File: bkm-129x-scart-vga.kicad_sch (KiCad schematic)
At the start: 58 parts, among them J1 DB15_Female_HighDensity_Mount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, J2 SCART-F, J3 SJ1-353XNG, J5 Conn_02x32_Row_Letter_Last, Q1 DTC144EKA, Q2 MMBT3904, SW1 PBH4UEENAGX, SW2 PBH4UEENAGX, U1 ADG1611, U2 THS7374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

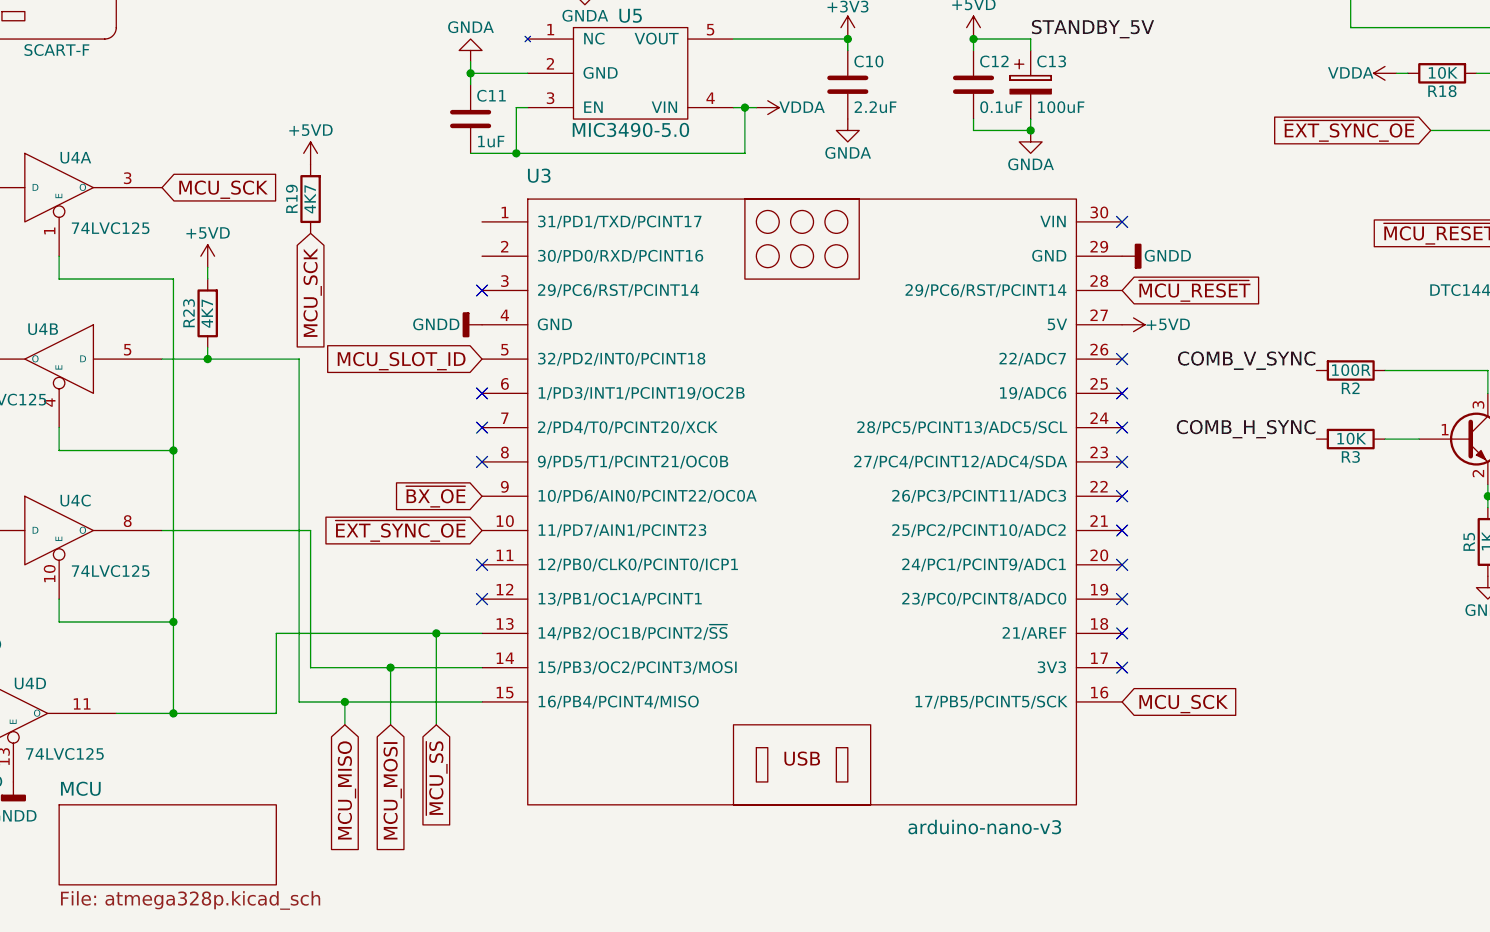
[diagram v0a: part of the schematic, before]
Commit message: Remove U3 Arduino Nano from PCB and schematic.
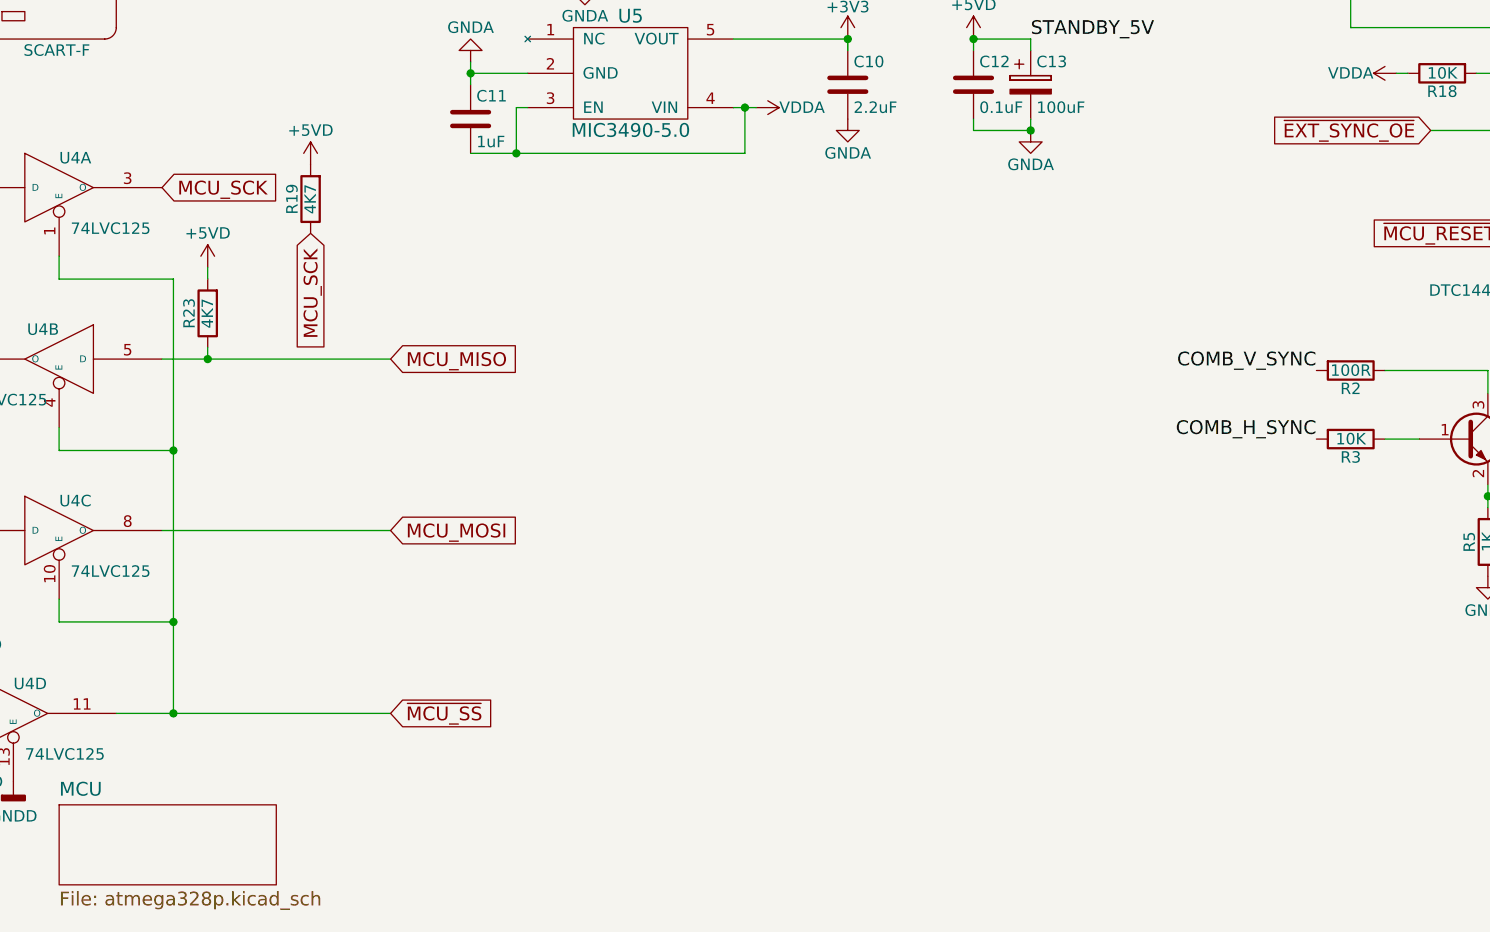
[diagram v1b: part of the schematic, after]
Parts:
- removed U3: arduino-nano-v3, arduino-nano-v3:arduino-nano-v3, symbol arduino-nano-v3:arduino-nano-v3
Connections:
- no-connect marks 53 -> 36

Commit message: Change U4 footprint to TSSOP-14 (74LVC125AD.112).
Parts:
- U4: footprint Package_SO:TSSOP-14_4.4x5mm_P0.65mm -> Package_SO:SOIC-14_3.9x8.7mm_P1.27mm
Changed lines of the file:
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@@
 			)
 		)
-		(property "Footprint" "Package_SO:TSSOP-14_4.4x5mm_P0.65mm"
+		(property "Footprint" "Package_SO:SOIC-14_3.9x8.7mm_P1.27mm"
 			(at 46.99 116.84 0)
 			(effects
@@
 			)
 		)
-		(property "Footprint" "Package_SO:TSSOP-14_4.4x5mm_P0.65mm"
+		(property "Footprint" "Package_SO:SOIC-14_3.9x8.7mm_P1.27mm"
 			(at 46.99 135.89 0)
 			(effects
@@
 			)
 		)
-		(property "Footprint" "Package_SO:TSSOP-14_4.4x5mm_P0.65mm"
+		(property "Footprint" "Package_SO:SOIC-14_3.9x8.7mm_P1.27mm"
 			(at 46.99 154.94 0)
 			(effects
@@
 			)
 		)
-		(property "Footprint" "Package_SO:TSSOP-14_4.4x5mm_P0.65mm"
+		(property "Footprint" "Package_SO:SOIC-14_3.9x8.7mm_P1.27mm"
 			(at 41.91 175.26 0)
 			(effects
